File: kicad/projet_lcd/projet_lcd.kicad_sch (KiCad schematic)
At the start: 0 parts

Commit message: EOD
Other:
- sheet stm32 renamed STM32
- added sheet Memory (Memory.kicad_sch)
- added sheet SD Card (USB.kicad_sch)
- sheet STM32 ports: added ETH_CRS_DV, ETH_MDC, ETH_MDIO, ETH_REF_CLK, ETH_RXD0, ETH_RXD1, ETH_TXD0, ETH_TXD1, ETH_TXEN, I2C_SCL, I2C_SDA, SDMMC_CLK, SDMMC_CMD, SDMMC_D0, SDMMC_D1, SDMMC_D2, SDMMC_D3, SDMMC_DETECT, SPI_MISO, SPI_MOSI, SPI_SCK, ~{NETWRK_RST}; removed RMII_CRS_DV, RMII_MDC, RMII_MDIO, RMII_REFCLK, RMII_RXD0, RMII_RXD1, RMII_TXD0, RMII_TXD1, RMII_TXEN, UDB_DM, UDB_DP, ~{RST}

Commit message: cleanup
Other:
- added sheet IO Connectors (io_connectors.kicad_sch)
- sheet SD Card: file USB.kicad_sch -> SD_Card.kicad_sch
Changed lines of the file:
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@@
+	(wire
+		(pts
+			(xy 96 63) (xy 105 63)
+		)
+		(stroke
+			(width 0)
+			(type default)
+		)
+	)
 	(wire
 		(pts
@@
 	(wire
 		(pts
+			(xy 96 69) (xy 105 69)
+		)
+		(stroke
+			(width 0)
+			(type default)
+		)
+	)
+	(wire
+		(pts
 			(xy 164 82) (xy 179 82)
 		)
@@
 	(wire
 		(pts
+			(xy 96 66) (xy 105 66)
+		)
+		(stroke
+			(width 0)
+			(type default)
+		)
+	)
+	(wire
+		(pts
 			(xy 204 96) (xy 204 110)
 		)
@@
 	(wire
 		(pts
+			(xy 96 77) (xy 105 77)
+		)
+		(stroke
+			(width 0)
+			(type default)
+		)
+	)
+	(wire
+		(pts
 			(xy 213 96) (xy 213 110)
 		)
@@
 		(pts
 			(xy 153 109) (xy 153 127)
+		)
+		(stroke
+			(width 0)
+			(type default)
+		)
+	)
+	(wire
+		(pts
+			(xy 96 74) (xy 105 74)
 		)
 		(stroke
@@
 	)
 	(sheet
+		(at 42 60)
+		(size 54 21)
+		(exclude_from_sim no)
+		(in_bom yes)
+		(on_board yes)
+		(dnp no)
+		(fields_autoplaced yes)
+		(stroke
+			(width 0.1524)
+			(type solid)
+		)
+		(fill
+			(color 0 0 0 0.0000)
+		)
+		(property "Sheetname" "IO Connectors"
+			(at 42 59.2884 0)
+			(effects
+				(font
+					(size 1.27 1.27)
+				)
+				(justify left bottom)
+			)
+		)
+		(property "Sheetfile" "io_connectors.kicad_sch"
+			(at 42 81.5846 0)
+			(effects
+				(font
+					(size 1.27 1.27)
+				)
+				(justify left top)
+			)
+		)
+		(pin "SPI_MOSI" input
+			(at 96 66 0)
+			(effects
+				(font
+					(size 1.27 1.27)
+				)
+				(justify right)
+			)
+		)
+		(pin "SPI_MISO" output
+			(at 96 69 0)
+			(effects
+				(font
+					(size 1.27 1.27)
+				)
+				(justify right)
+			)
+		)
+		(pin "I2C_SCL" input
+			(at 96 77 0)
+			(effects
+				(font
+					(size 1.27 1.27)
+				)
+				(justify right)
+			)
+		)
+		(pin "I2C_SDA" bidirectional
+			(at 96 74 0)
+			(effects
+				(font
+					(size 1.27 1.27)
+				)
+				(justify right)
+			)
+		)
+		(pin "SPI_SCK" input
+			(at 96 63 0)
+			(effects
+				(font
+					(size 1.27 1.27)
+				)
+				(justify right)
+			)
+		)
+		(instances
+			(project "projet_lcd"
+				(path "/b3ce22de-813e-4a84-80c2-bec39c904000"
+					(page "7")
+				)
+			)
+		)
+	)
+	(sheet
 		(at 104 127)
 		(size 60 29)
@@
 			)
 		)
-		(property "Sheetfile" "USB.kicad_sch"
+		(property "Sheetfile" "SD_Card.kicad_sch"
 			(at 104 156.5846 0)
 			(effects
@@
 		(on_board yes)
 		(dnp no)
-		(fields_autoplaced yes)
 		(stroke
 			(width 0.1524)
@@
 		)
 		(property "Sheetfile" "Memory.kicad_sch"
-			(at 124 55.5846 0)
-			(effects
-				(font
+			(at 141 39 0)
+			(effects
+				(font

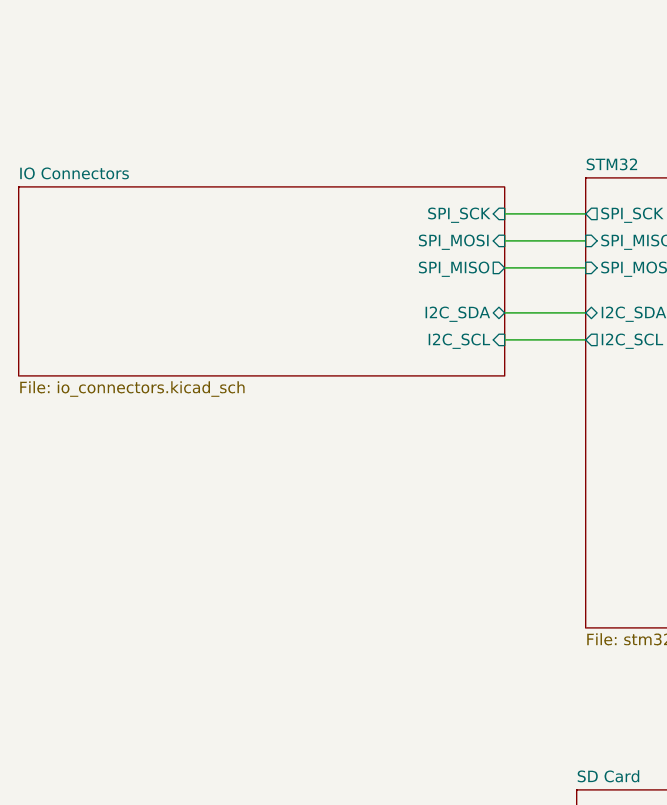
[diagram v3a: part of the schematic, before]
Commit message: cleaning up ERC alerts
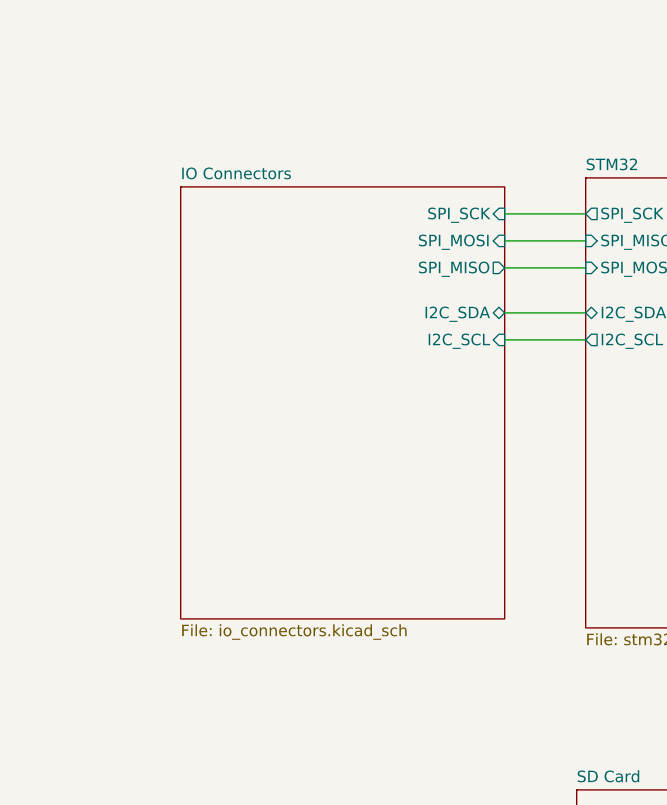
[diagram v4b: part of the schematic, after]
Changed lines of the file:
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@@
 	)
 	(sheet
-		(at 42 60)
-		(size 54 21)
+		(at 60 60)
+		(size 36 48)
 		(exclude_from_sim no)
 		(in_bom yes)
@@
 		)
 		(property "Sheetname" "IO Connectors"
-			(at 42 59.2884 0)
+			(at 60 59.2884 0)
 			(effects
 				(font
@@
 		)
 		(property "Sheetfile" "io_connectors.kicad_sch"
-			(at 42 81.5846 0)
+			(at 60 108.5846 0)
 			(effects
 				(font

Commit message: on avance !
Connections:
- no-connect marks 0 -> 1
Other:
- sheet IO Connectors ports: added DISPLAY_CS, DISPLAY_PWM, DISPLAY_RS, DISPLAY_RST, DISPLAY_SCL, DISPLAY_SDA, OUTPUT_0, OUTPUT_1, OUTPUT_2, OUTPUT_3, OUTPUT_4, OUTPUT_5, OUTPUT_6, OUTPUT_7, OUTPUT_8, OUTPUT_9; removed none
- sheet STM32 ports: added DISPLAY_CLK, DISPLAY_CS, DISPLAY_MISO, DISPLAY_MOSI, DISPLAY_PWM, DISPLAY_RS, DISPLAY_RST, OUTPUT_0, OUTPUT_1, OUTPUT_2, OUTPUT_3, OUTPUT_4, OUTPUT_5, OUTPUT_6, OUTPUT_7, OUTPUT_8, OUTPUT_9; removed none

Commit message: DRC / ERC ok
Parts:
- added LOGO2: ~, Graphics:Rancune_15mm, symbol Graphics:Logo_Rancune
- added MH1, MH2, MH3, MH4: ~, PCB_Utils:MH_M3, symbol PCB_Utils:MH
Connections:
- new net GND: MH1.1, MH2.1, MH3.1, MH4.1
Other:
- sheet IO Connectors ports: added LED_1, LED_2, LED_3, LED_4; removed none
- sheet STM32 ports: added LED_1, LED_2, LED_3, LED_4; removed none
